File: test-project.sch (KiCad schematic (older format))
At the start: 35 parts, among them P1 CONN_01X06, P2 CONN_01X02, U1 74HC14, U2 OP275, U3 74LS163, U4 27C512

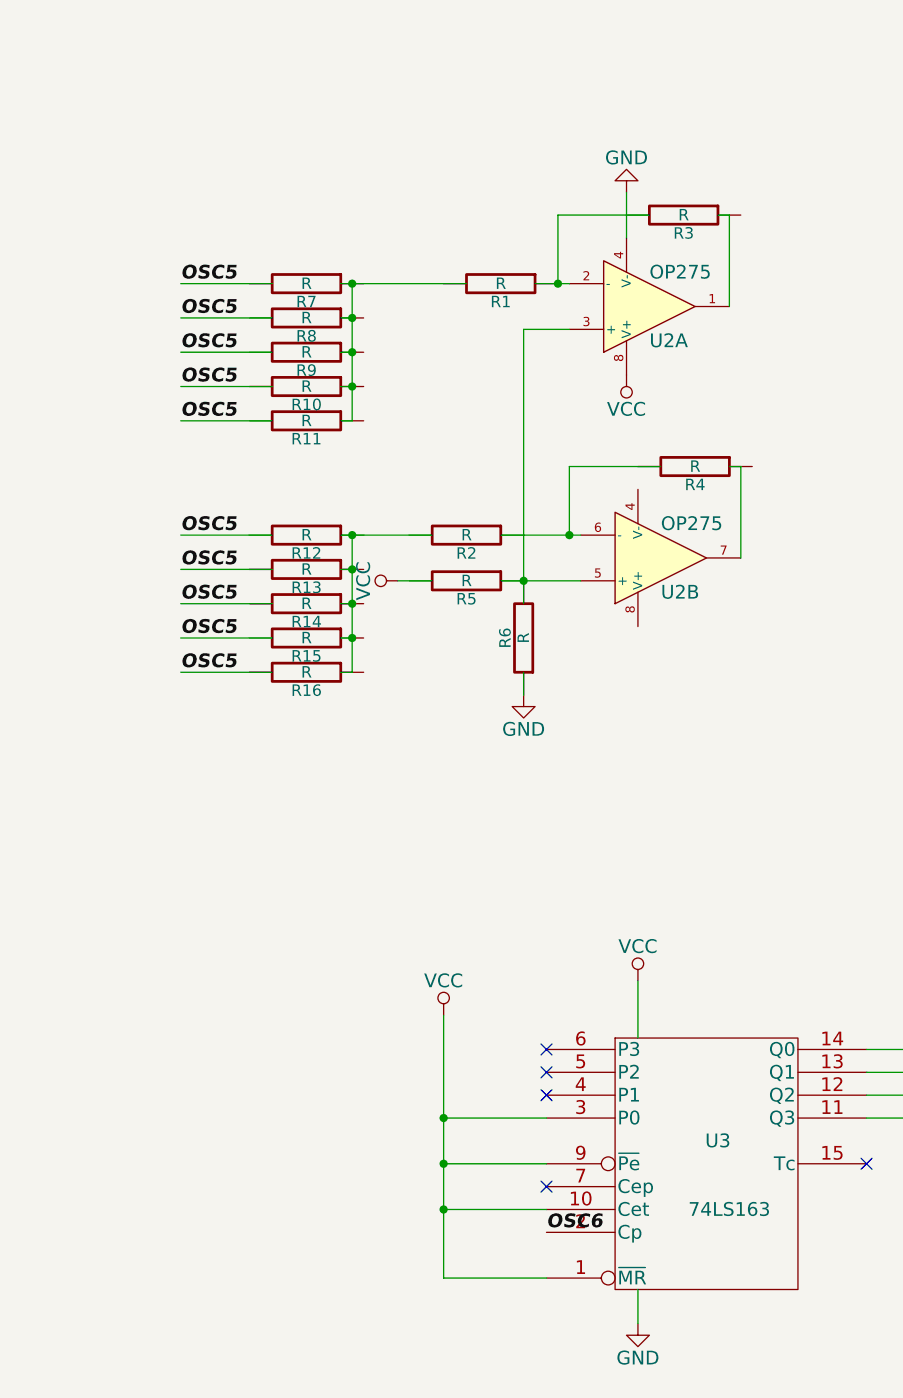
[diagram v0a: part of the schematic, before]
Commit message: fixed some missed connections on schematic
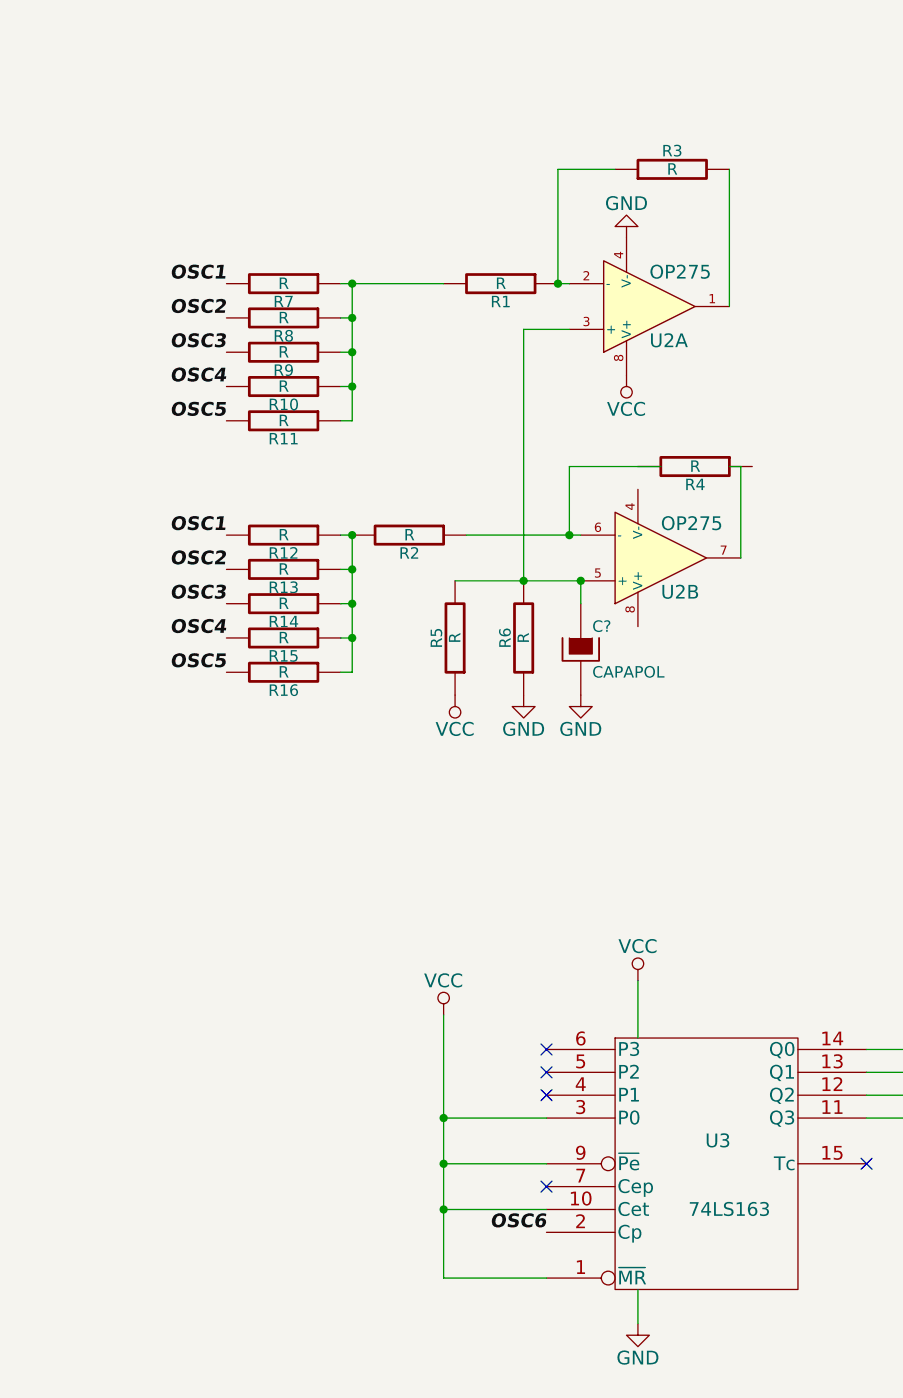
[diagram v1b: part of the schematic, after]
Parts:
- added C?: CAPAPOL, symbol CAPAPOL
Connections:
- wire segments 93 -> 80
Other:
- moved on the sheet: R10, R11, R12, R13, R14, R15, R16, R2, R3, R5, R7, R8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
